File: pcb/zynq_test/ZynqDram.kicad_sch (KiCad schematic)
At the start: 44 parts, among them U202 XC7Z020-2CLG400I, U401 MT41K256M16TW-107, U402 MT41K256M16TW-107

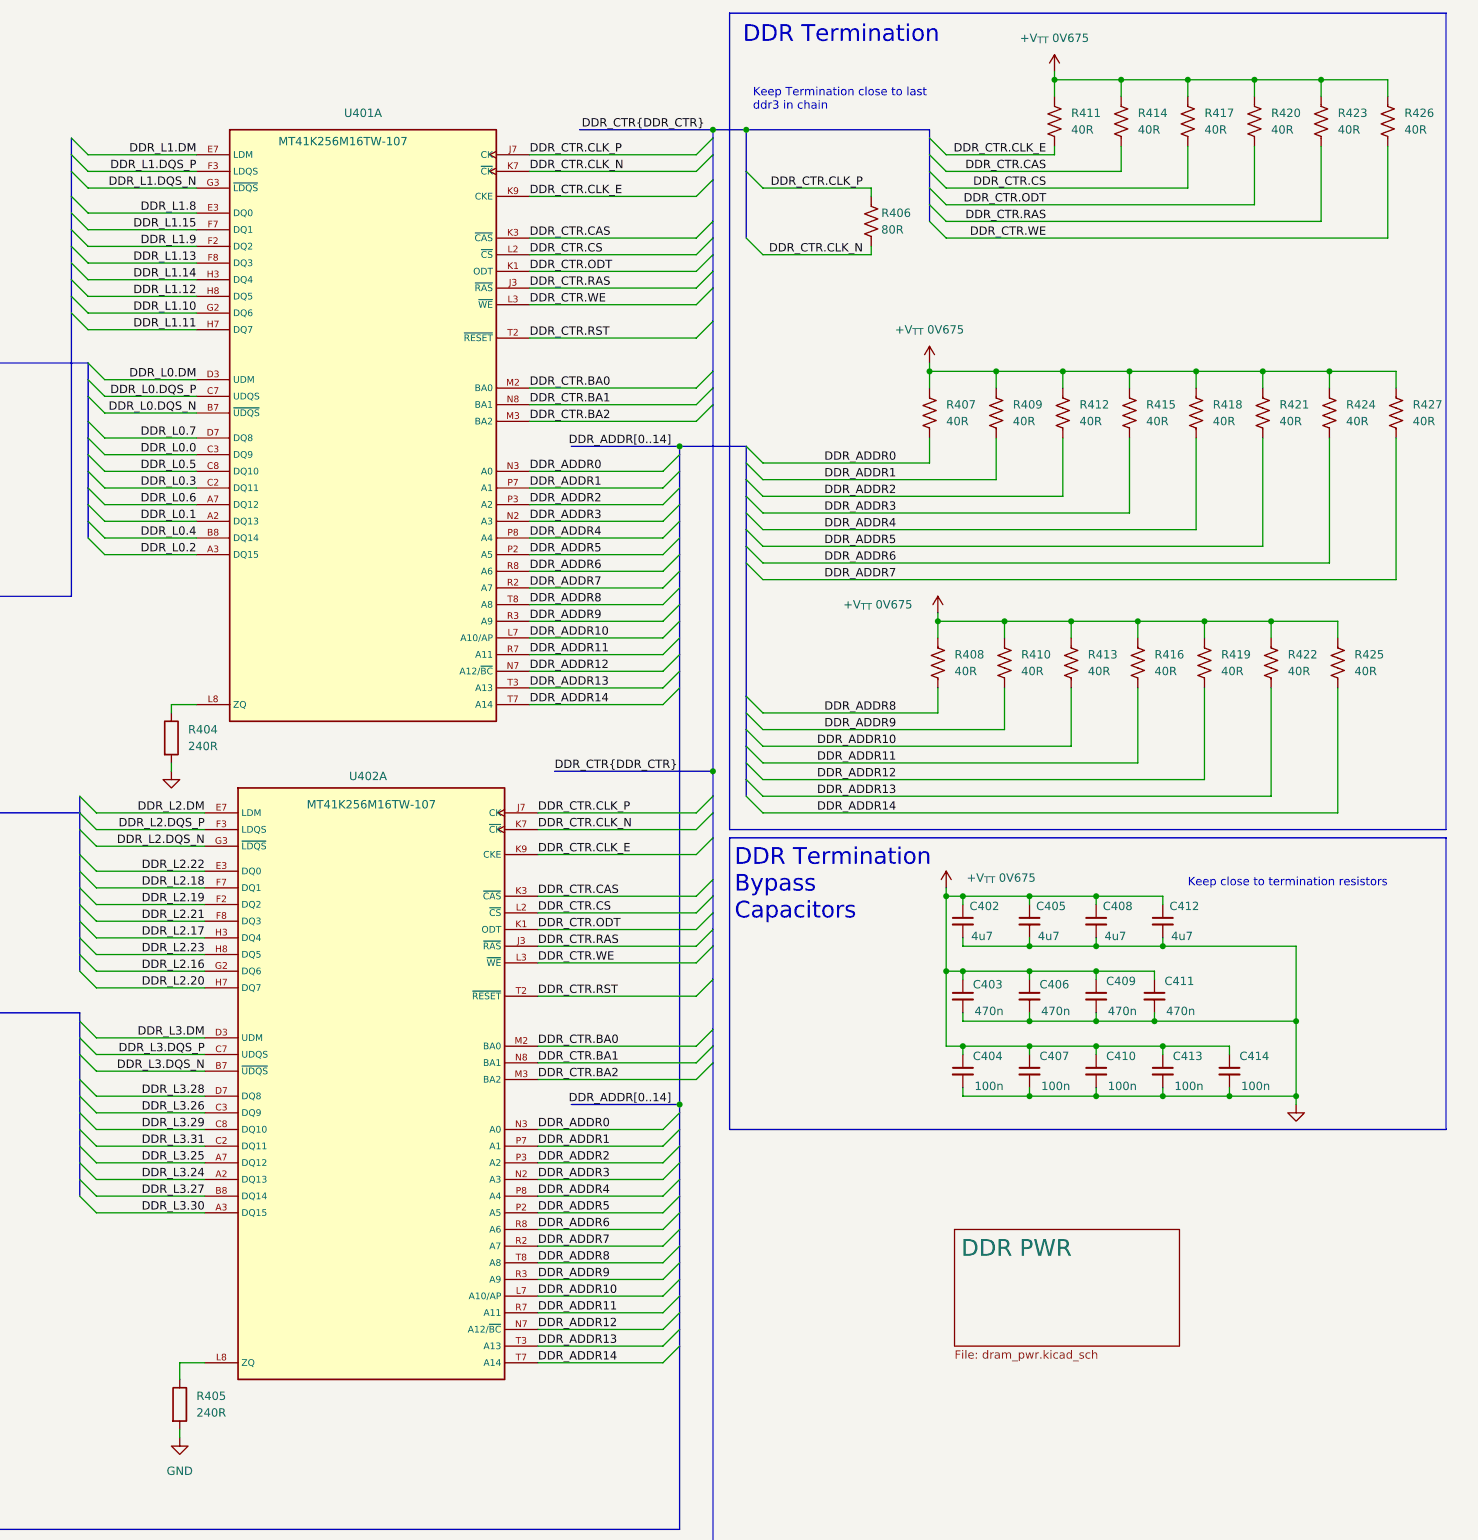
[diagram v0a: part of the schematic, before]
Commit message: DDR routed
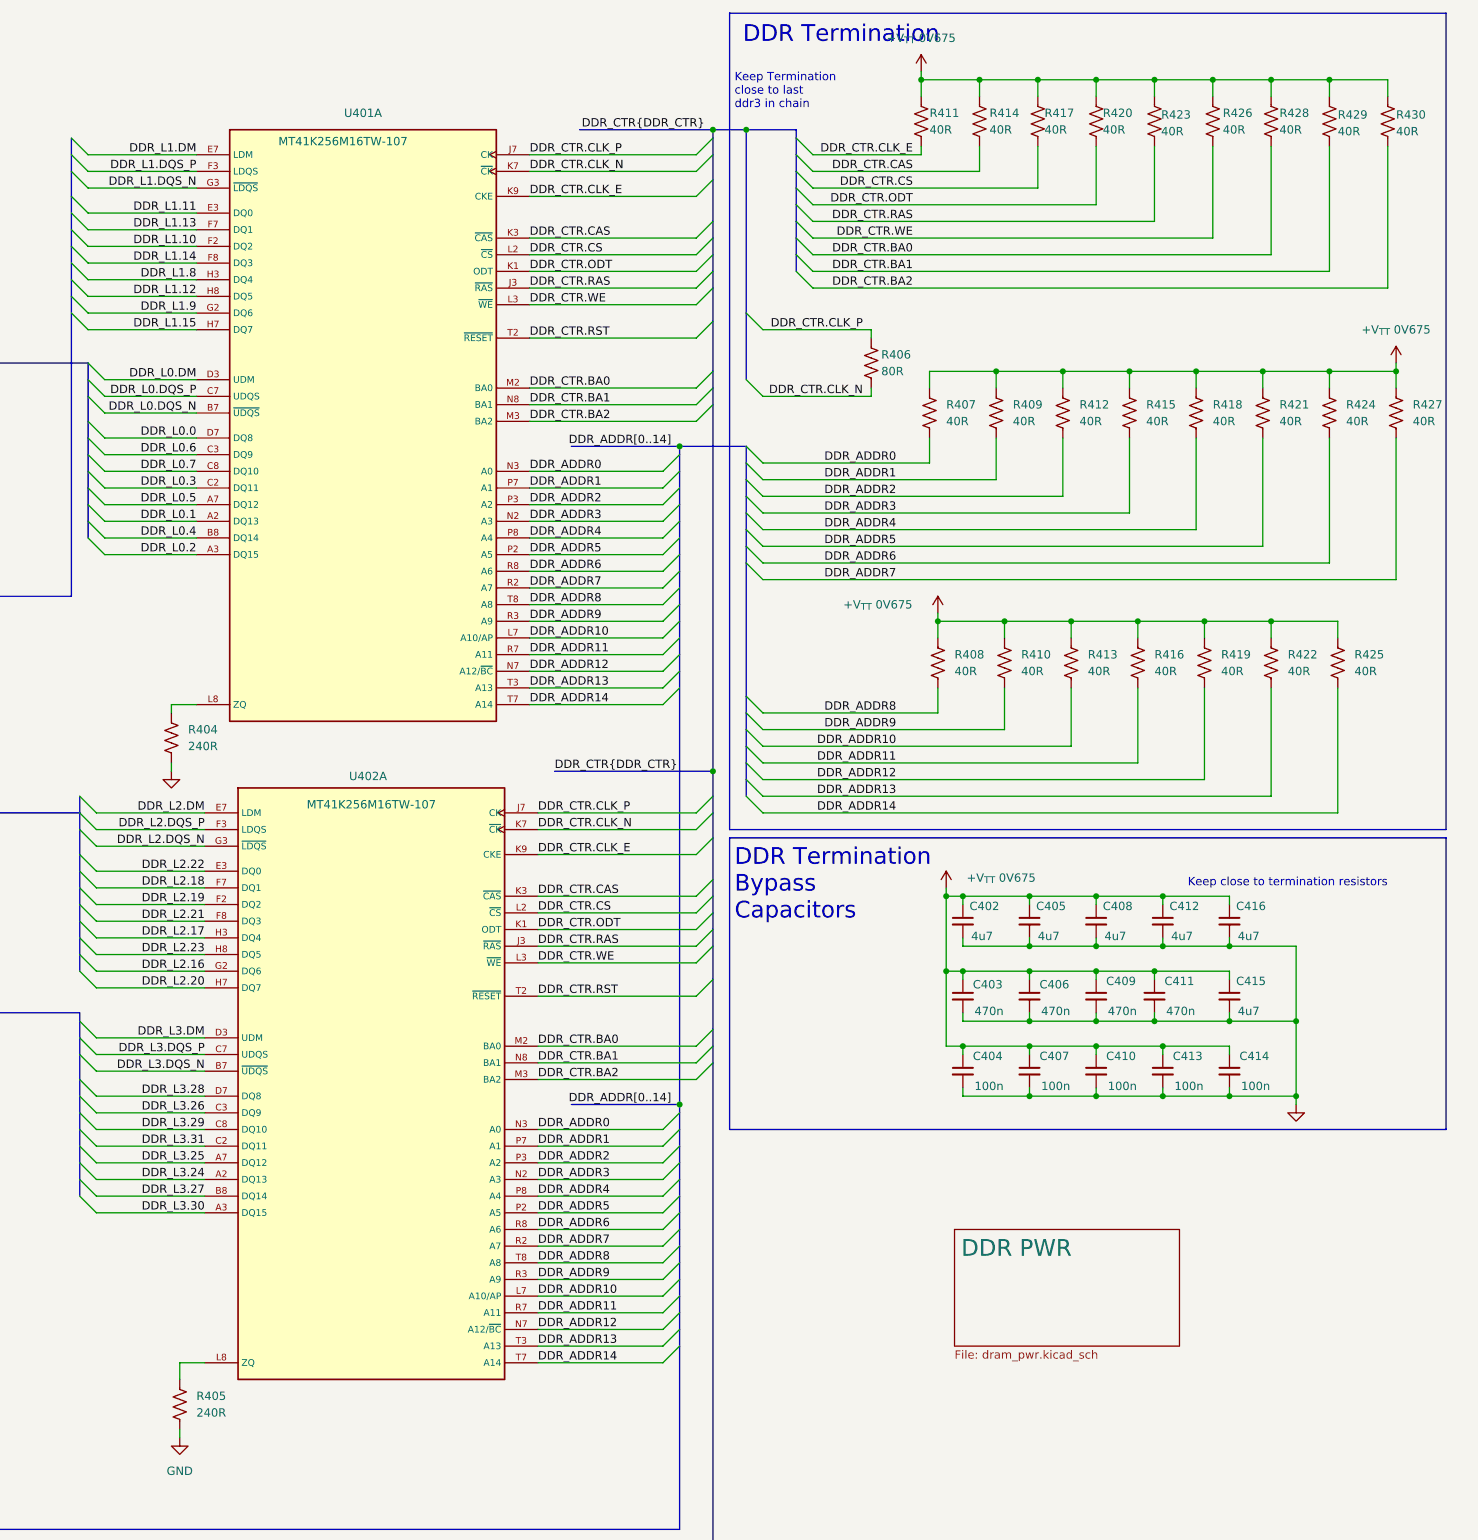
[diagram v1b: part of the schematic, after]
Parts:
- added C415, C416: 4u7, Capacitor_SMD:C_0402_1005Metric, symbol Device:C_Small
- added R428, R429, R430: 40R, Resistor_SMD:R_0402_1005Metric, symbol Device:R_US
- C401, C402, C403, C404, C405, C406, C407, C408, C409, C410, C411, C412, C413, C414: footprint (none) -> Capacitor_SMD:C_0402_1005Metric
- R401, R402, R406: footprint (none) -> Resistor_SMD:R_0201_0603Metric
- R403, R407, R408, R409, R410, R411, R412, R413, R414, R415, R416, R417, R418, R419, R420, R421, R422, R423, R424, R425, R426, R427: footprint (none) -> Resistor_SMD:R_0402_1005Metric
- R404, R405: footprint (none) -> Resistor_SMD:R_0402_1005Metric; symbol Device:R -> Device:R_US
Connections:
- net +V_{TT} 0V675: now also C415.1, C416.1, R428.1, R429.1, R430.1
- net DDR_CTR.BA0: now also R428.2
- net DDR_CTR.BA1: now also R429.2
- net DDR_CTR.BA2: now also R430.2
- net DDR_L0.0: now also U401.D7 (DQ8); no longer U401.C3 (DQ9)
- net DDR_L0.5: now also U401.A7 (DQ12); no longer U401.C8 (DQ10)
- net DDR_L0.6: now also U401.C3 (DQ9); no longer U401.A7 (DQ12)
- net DDR_L0.7: now also U401.C8 (DQ10); no longer U401.D7 (DQ8)
- net DDR_L1.10: now also U401.F2 (DQ2); no longer U401.G2 (DQ6)
- net DDR_L1.11: now also U401.E3 (DQ0); no longer U401.H7 (DQ7)
- net DDR_L1.13: now also U401.F7 (DQ1); no longer U401.F8 (DQ3)
- net DDR_L1.14: now also U401.F8 (DQ3); no longer U401.H3 (DQ4)
- net DDR_L1.15: now also U401.H7 (DQ7); no longer U401.F7 (DQ1)
- net DDR_L1.8: now also U401.H3 (DQ4); no longer U401.E3 (DQ0)
- net DDR_L1.9: now also U401.G2 (DQ6); no longer U401.F2 (DQ2)
- net GND: now also C415.2, C416.2
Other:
- moved on the sheet: R406, R411, R414, R417, R420, R423, R426

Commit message: Almost done with BOM
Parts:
- renumbered C416 to C414, C414 to C416, R411 to R407, R407 to R408, R408 to R409, R414 to R410, R409 to R411, R410 to R412, R417 to R413, R412 to R414, R413 to R415, R420 to R416, R415 to R417, R416 to R418, R423 to R419, R418 to R420, R419 to R421, R426 to R422, R421 to R423, R428 to R424, R422 to R425, R429 to R426, R424 to R427, R425 to R428, R430 to R429, R427 to R430
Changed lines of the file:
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@@
 		(dnp no)
 		(fields_autoplaced yes)
-		(property "Reference" "#PWR0412"
+		(property "Reference" "#PWR0411"
 			(at 383.54 186.69 0)
 			(effects
@@
 			(project "zynq_test"
 				(path "/0637578d-4ce5-4d31-b973-2de977269ea5/920e1ce4-7460-4edb-8921-03ce78d5c203"
-					(reference "#PWR0412")
+					(reference "#PWR0411")
 					(unit 1)
 				)
@@
 		(dnp no)
 		(fields_autoplaced yes)
-		(property "Reference" "#PWR0411"
+		(property "Reference" "#PWR0408"
 			(at 326.39 26.67 0)
 			(effects
@@
 			(project ""
 				(path "/0637578d-4ce5-4d31-b973-2de977269ea5/920e1ce4-7460-4edb-8921-03ce78d5c203"
-					(reference "#PWR0411")
+					(reference "#PWR0408")
 					(unit 1)
 				)
@@
 		(dnp no)
 		(fields_autoplaced yes)
-		(property "Reference" "R409"
+		(property "Reference" "R411"
 			(at 340.36 73.6599 0)
 			(effects
@@
 			(project "zynq_test"
 				(path "/0637578d-4ce5-4d31-b973-2de977269ea5/920e1ce4-7460-4edb-8921-03ce78d5c203"
-					(reference "R409")
+					(reference "R411")
 					(unit 1)
 				)
@@
 		(dnp no)
 		(fields_autoplaced yes)
-		(property "Reference" "R425"
+		(property "Reference" "R428"
 			(at 392.43 111.7599 0)
 			(effects
@@
 			(project "zynq_test"
 				(path "/0637578d-4ce5-4d31-b973-2de977269ea5/920e1ce4-7460-4edb-8921-03ce78d5c203"
-					(reference "R425")
+					(reference "R428")
 					(unit 1)
 				)
@@
 		(on_board yes)
 		(dnp no)
-		(property "Reference" "R411"
+		(property "Reference" "R407"
 			(at 327.66 29.21 0)
 			(effects
@@
 			(project "zynq_test"
 				(path "/0637578d-4ce5-4d31-b973-2de977269ea5/920e1ce4-7460-4edb-8921-03ce78d5c203"
-					(reference "R411")
+					(reference "R407")
 					(unit 1)
 				)
@@
 		(on_board yes)
 		(dnp no)
-		(property "Reference" "R417"
+		(property "Reference" "R413"
 			(at 345.186 29.21 0)
 			(effects
@@
 			(project "zynq_test"
 				(path "/0637578d-4ce5-4d31-b973-2de977269ea5/920e1ce4-7460-4edb-8921-03ce78d5c203"
-					(reference "R417")
+					(reference "R413")
 					(unit 1)
 				)
@@
 		(on_board yes)
 		(dnp no)
-		(property "Reference" "R420"
+		(property "Reference" "R416"
 			(at 354.076 29.21 0)
 			(effects
@@
 			(project "zynq_test"
 				(path "/0637578d-4ce5-4d31-b973-2de977269ea5/920e1ce4-7460-4edb-8921-03ce78d5c203"
-					(reference "R420")
+					(reference "R416")
 					(unit 1)
 				)
@@
 		(dnp no)
 		(fields_autoplaced yes)
-		(property "Reference" "R424"
+		(property "Reference" "R427"
 			(at 391.16 73.6599 0)
 			(effects
@@
 			(project "zynq_test"
 				(path "/0637578d-4ce5-4d31-b973-2de977269ea5/920e1ce4-7460-4edb-8921-03ce78d5c203"
-					(reference "R424")
+					(reference "R427")
 					(unit 1)
 				)
@@
 		(dnp no)
 		(fields_autoplaced yes)
-		(property "Reference" "R410"
+		(property "Reference" "R412"
 			(at 341.63 111.7599 0)
 			(effects
@@
 			(project "zynq_test"
 				(path "/0637578d-4ce5-4d31-b973-2de977269ea5/920e1ce4-7460-4edb-8921-03ce78d5c203"
-					(reference "R410")
+					(reference "R412")
 					(unit 1)
 				)
@@
 		(dnp no)
 		(fields_autoplaced yes)
-		(property "Reference" "R415"
+		(property "Reference" "R417"
 			(at 360.68 73.6599 0)
 			(effects
@@
 			(project "zynq_test"
 				(path "/0637578d-4ce5-4d31-b973-2de977269ea5/920e1ce4-7460-4edb-8921-03ce78d5c203"
-					(reference "R415")
+					(reference "R417")
 					(unit 1)
 				)
@@
 		(dnp no)
 		(fields_autoplaced yes)
-		(property "Reference" "R418"
+		(property "Reference" "R420"
 			(at 370.84 73.6599 0)
 			(effects
@@
 			(project "zynq_test"
 				(path "/0637578d-4ce5-4d31-b973-2de977269ea5/920e1ce4-7460-4edb-8921-03ce78d5c203"
-					(reference "R418")
+					(reference "R420")
 					(unit 1)
 				)
@@
 		(on_board yes)
 		(dnp no)
-		(property "Reference" "R428"
+		(property "Reference" "R424"
 			(at 381 29.21 0)
 			(effects
@@
 			(project "zynq_test"
 				(path "/0637578d-4ce5-4d31-b973-2de977269ea5/920e1ce4-7460-4edb-8921-03ce78d5c203"
-					(reference "R428")
+					(reference "R424")
 					(unit 1)
 				)
@@
 		(dnp no)
 		(fields_autoplaced yes)
-		(property "Reference" "R422"
+		(property "Reference" "R425"
 			(at 382.27 111.7599 0)
 			(effects
@@
 			(project "zynq_test"
 				(path "/0637578d-4ce5-4d31-b973-2de977269ea5/920e1ce4-7460-4edb-8921-03ce78d5c203"
-					(reference "R422")
+					(reference "R425")
 					(unit 1)
 				)
@@
 		(dnp no)
 		(fields_autoplaced yes)
-		(property "Reference" "C416"
+		(property "Reference" "C414"
 			(at 374.396 150.114 0)
 			(effects
@@
 			(project "zynq_test"
 				(path "/0637578d-4ce5-4d31-b973-2de977269ea5/920e1ce4-7460-4edb-8921-03ce78d5c203"
-					(reference "C416")
+					(reference "C414")
 					(unit 1)
 				)
@@
 		(dnp no)
 		(fields_autoplaced yes)
-		(property "Reference" "R419"
+		(property "Reference" "R421"
 			(at 372.11 111.7599 0)
 			(effects
@@
 			(project "zynq_test"
 				(path "/0637578d-4ce5-4d31-b973-2de977269ea5/920e1ce4-7460-4edb-8921-03ce78d5c203"
-					(reference "R419")
+					(reference "R421")
 					(unit 1)
 				)
@@
 		(on_board yes)
 		(dnp no)
-		(property "Reference" "R423"
+		(property "Reference" "R419"
 			(at 362.966 29.464 0)
 			(effects
@@
 			(project "zynq_test"
 				(path "/0637578d-4ce5-4d31-b973-2de977269ea5/920e1ce4-7460-4edb-8921-03ce78d5c203"
-					(reference "R423")
+					(reference "R419")
 					(unit 1)
 				)
@@
 		(dnp no)
 		(fields_autoplaced yes)
-		(property "Reference" "#PWR0408"
+		(property "Reference" "#PWR0412"
 			(at 398.78 71.12 0)
 			(effects
@@
 			(project "zynq_test"
 				(path "/0637578d-4ce5-4d31-b973-2de977269ea5/920e1ce4-7460-4edb-8921-03ce78d5c203"
-					(reference "#PWR0408")
+					(reference "#PWR0412")
 					(unit 1)
 				)
@@
 		(dnp no)
 		(fields_autoplaced yes)
-		(property "Reference" "R413"
+		(property "Reference" "R415"
 			(at 351.79 111.7599 0)
 			(effects
@@
 			(project "zynq_test"
 				(path "/0637578d-4ce5-4d31-b973-2de977269ea5/920e1ce4-7460-4edb-8921-03ce78d5c203"
-					(reference "R413")
+					(reference "R415")
 					(unit 1)
 				)
@@
 		(on_board yes)
 		(dnp no)
-		(property "Reference" "R426"
+		(property "Reference" "R422"
 			(at 372.364 29.21 0)
 			(effects
@@
 			(project "zynq_test"
 				(path "/0637578d-4ce5-4d31-b973-2de977269ea5/920e1ce4-7460-4edb-8921-03ce78d5c203"
-					(reference "R426")
+					(reference "R422")
 					(unit 1)
 				)
@@
 		(on_board yes)
 		(dnp no)
-		(property "Reference" "R430"
+		(property "Reference" "R429"
 			(at 398.78 29.464 0)
 			(effects
@@
 			(project "zynq_test"
 				(path "/0637578d-4ce5-4d31-b973-2de977269ea5/920e1ce4-7460-4edb-8921-03ce78d5c203"
-					(reference "R430")
+					(reference "R429")
 					(unit 1)
 				)
@@
 		(dnp no)
 		(fields_autoplaced yes)
-		(property "Reference" "C414"
+		(property "Reference" "C416"
 			(at 374.904 172.974 0)
 			(effects
@@
 			(project "zynq_test"
 				(path "/0637578d-4ce5-4d31-b973-2de977269ea5/920e1ce4-7460-4edb-8921-03ce78d5c203"
-					(reference "C414")
+					(reference "C416")
 					(unit 1)
 				)
@@
 		(on_board yes)
 		(dnp no)
-		(property "Reference" "R414"
+		(property "Reference" "R410"
 			(at 336.804 29.21 0)
 			(effects
@@
 			(project "zynq_test"
 				(path "/0637578d-4ce5-4d31-b973-2de977269ea5/920e1ce4-7460-4edb-8921-03ce78d5c203"
-					(reference "R414")
+					(reference "R410")
 					(unit 1)
 				)
@@
 		(dnp no)
 		(fields_autoplaced yes)
-		(property "Reference" "R421"
+		(property "Reference" "R423"
 			(at 381 73.6599 0)
 			(effects
@@
 			(project "zynq_test"
 				(path "/0637578d-4ce5-4d31-b973-2de977269ea5/920e1ce4-7460-4edb-8921-03ce78d5c203"
-					(reference "R421")
+					(reference "R423")
 					(unit 1)
 				)
@@
 		(dnp no)
 		(fields_autoplaced yes)
-		(property "Reference" "R427"
+		(property "Reference" "R430"
 			(at 401.32 73.6599 0)
 			(effects
@@
 			(project "zynq_test"
 				(path "/0637578d-4ce5-4d31-b973-2de977269ea5/920e1ce4-7460-4edb-8921-03ce78d5c203"
-					(reference "R427")
+					(reference "R430")
 					(unit 1)
 				)
@@
 		(on_board yes)
 		(dnp no)
-		(property "Reference" "R429"
+		(property "Reference" "R426"
 			(at 389.89 29.464 0)
 			(effects
@@
 			(project "zynq_test"
 				(path "/0637578d-4ce5-4d31-b973-2de977269ea5/920e1ce4-7460-4edb-8921-03ce78d5c203"
-					(reference "R429")
+					(reference "R426")
 					(unit 1)
 				)
@@
 		(dnp no)
 		(fields_autoplaced yes)
-		(property "Reference" "R416"
+		(property "Reference" "R418"
 			(at 361.95 111.7599 0)
 			(effects
@@
 			(project "zynq_test"
 				(path "/0637578d-4ce5-4d31-b973-2de977269ea5/920e1ce4-7460-4edb-8921-03ce78d5c203"
-					(reference "R416")
+					(reference "R418")
 					(unit 1)
 				)
@@
 		(dnp no)
 		(fields_autoplaced yes)
-		(property "Reference" "R412"
+		(property "Reference" "R414"
 			(at 350.52 73.6599 0)
 			(effects
@@
 			(project "zynq_test"
 				(path "/0637578d-4ce5-4d31-b973-2de977269ea5/920e1ce4-7460-4edb-8921-03ce78d5c203"
-					(reference "R412")
+					(reference "R414")
 					(unit 1)
 				)
@@
 		(dnp no)
 		(fields_autoplaced yes)
-		(property "Reference" "R407"
+		(property "Reference" "R408"
 			(at 330.2 73.6599 0)
 			(effects
@@
 			(project "zynq_test"
 				(path "/0637578d-4ce5-4d31-b973-2de977269ea5/920e1ce4-7460-4edb-8921-03ce78d5c203"
-					(reference "R407")
+					(reference "R408")
 					(unit 1)
 				)
@@
 		(dnp no)
 		(fields_autoplaced yes)
-		(property "Reference" "R408"
+		(property "Reference" "R409"
 			(at 331.47 111.7599 0)
 			(effects
@@
 			(project "zynq_test"
 				(path "/0637578d-4ce5-4d31-b973-2de977269ea5/920e1ce4-7460-4edb-8921-03ce78d5c203"
-					(reference "R408")
+					(reference "R409")
 					(unit 1)
 				)

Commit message: Version sent to JLCPCB
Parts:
- C401, C403, C406, C409, C411: JLCPCB Part# (none) -> C88946; PART_NUMBER (none) -> GRM155R71A474KE01D
- C402, C405, C408, C412, C414, C415: JLCPCB Part# (none) -> C23733; PART_NUMBER (none) -> CL05A475MP5NRNC
- C404, C407, C410, C413, C416: JLCPCB Part# (none) -> C1525; PART_NUMBER (none) -> CL05B104KO5NNNC
- R401, R402, R406: JLCPCB Part# (none) -> C473438; PART_NUMBER (none) -> 0201WMF806JTEE
- R403: JLCPCB Part# (none) -> C327817; PART_NUMBER (none) -> MR04X4701FTL
- R404, R405: JLCPCB Part# (none) -> C131545; PART_NUMBER (none) -> RK73B1ETTP241J
- R407, R408, R409, R410, R411, R412, R413, R414, R415, R416, R417, R418, R419, R420, R421, R422, R423, R424, R425, R426, R427, R428, R429, R430: JLCPCB Part# (none) -> C116386; PART_NUMBER (none) -> ERJ2RKF40R2X
- U202: JLCPCB Part# (none) -> C569043; PART_NUMBER (none) -> XC7Z020-2CLG400I
- U401, U402: JLCPCB Part# (none) -> C367428; PART_NUMBER (none) -> MT41K256M16TW-107 IT:P
